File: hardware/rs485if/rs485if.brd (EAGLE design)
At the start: 84.3 x 51 mm, 79 parts, among them IC1 BSP75, IC2 PCA82C250SMD, IC4 78L05SMD, IC5 MAX481CSA, Q1 3M6864, T1 MKDSO_2.5/3_R, T2 MKDSO_2.5/3_R, T3 MKDSO_2.5/3_L, T4 MKDSO_2.5/3_L

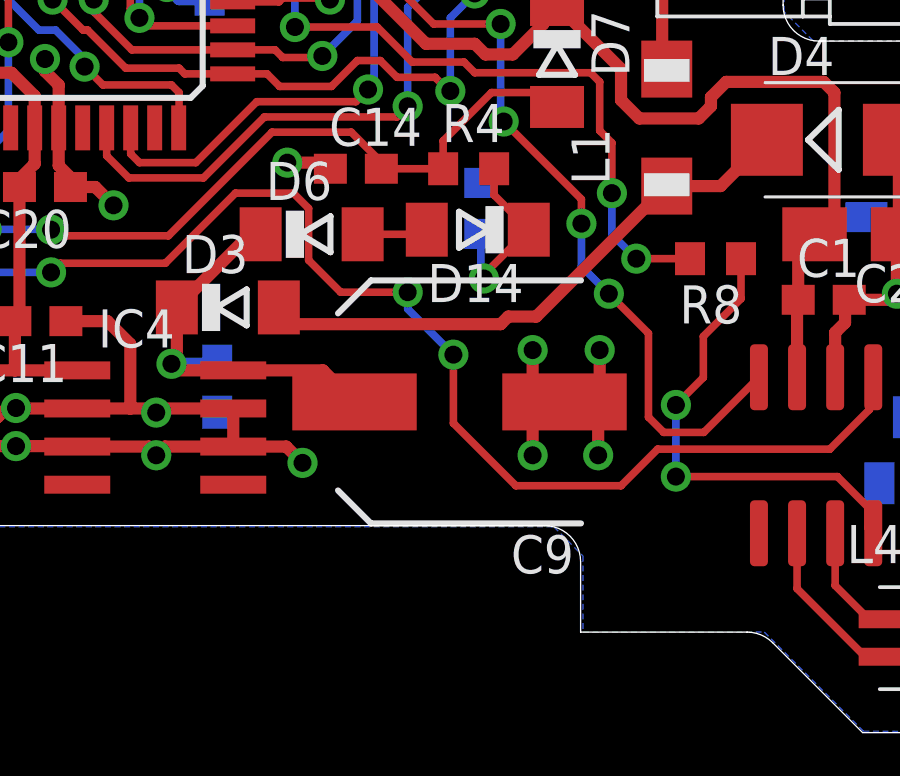
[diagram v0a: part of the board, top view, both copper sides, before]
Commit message: elko position move
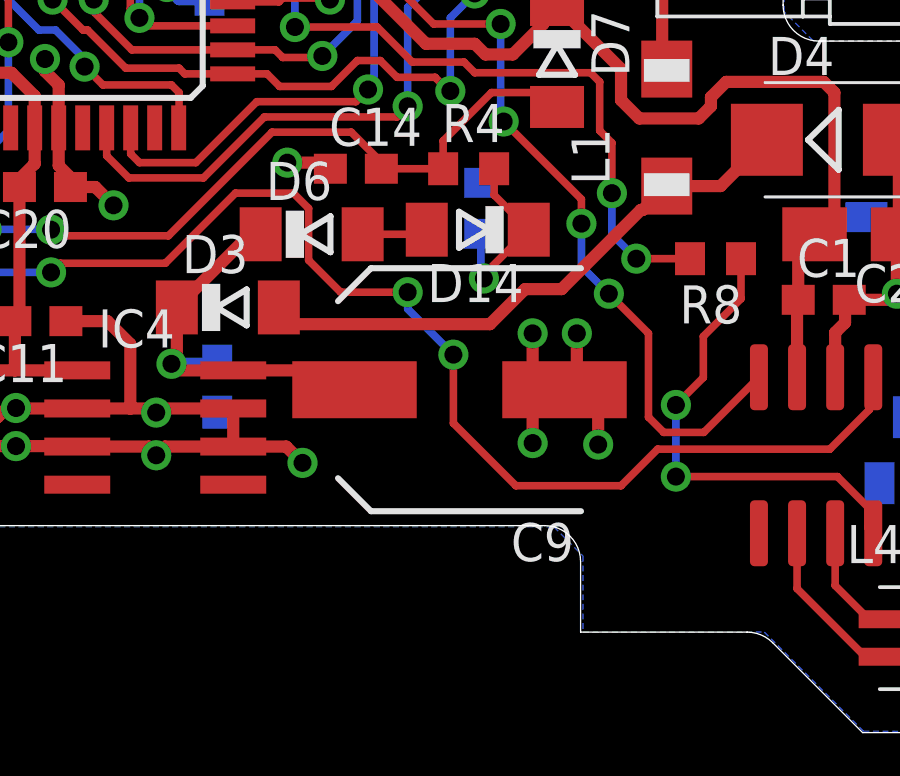
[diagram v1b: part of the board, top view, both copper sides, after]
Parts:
- moved C9 0.41 mm to (52.0, 10.9)
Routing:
- net GND: track 137.6 -> 136.0 mm
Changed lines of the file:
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@@
 <element name="D2" library="EagleLibrary_Wuerth_Elektronik_eiSos_V6_20140807" package="WE-TVS_SOT23-3L" value="WE-TVS_824021" x="66.9676" y="8.8566" rot="MR0"/>
 <element name="IC4" library="linear" package="SO08" value="78L05SMD" x="41.8776" y="9.6112" rot="R270"/>
-<element name="C9" library="rcl" package="SANYO-OSCON_SMD_E7" value="470µ/16V Würth Elektronik WCAP-ASLL 865060353009" x="52.0192" y="10.4648" rot="R180"/>
+<element name="C9" library="rcl" package="SANYO-OSCON_SMD_E7" value="470µ/16V Würth Elektronik WCAP-ASLL 865060353009" x="52.0192" y="10.8712" rot="R180"/>
 <element name="C10" library="resistor" package="C0603" value="100n" x="43.942" y="10.9728" rot="MR90"/>
 <element name="C11" library="resistor" package="C0603" value="100n" x="38.0492" y="13.1572" rot="R180"/>
@@
 <via x="19.9644" y="13.9192" extent="1-16" drill="0.6" shape="octagon"/>
 <via x="66.5988" y="14.0716" extent="1-16" drill="0.6" shape="octagon"/>
-<via x="54.4576" y="8.6868" extent="1-16" drill="0.6" shape="octagon"/>
-<via x="56.642" y="8.6868" extent="1-16" drill="0.6" shape="octagon"/>
-<via x="56.6928" y="12.192" extent="1-16" drill="0.6" shape="octagon"/>
-<via x="54.4576" y="12.192" extent="1-16" drill="0.6" shape="octagon"/>
-<wire x1="54.4576" y1="12.192" x2="54.4576" y2="10.4648" width="0.4064" layer="1"/>
-<wire x1="56.6928" y1="12.192" x2="56.6928" y2="10.4648" width="0.4064" layer="1"/>
-<wire x1="56.6928" y1="10.4648" x2="55.5192" y2="10.4648" width="0.4064" layer="1"/>
-<wire x1="56.642" y1="8.6868" x2="56.642" y2="10.4648" width="0.4064" layer="1"/>
-<wire x1="56.642" y1="10.4648" x2="55.5192" y2="10.4648" width="0.4064" layer="1"/>
-<wire x1="54.4576" y1="8.6868" x2="54.4576" y2="10.4648" width="0.4064" layer="1"/>
-<wire x1="54.4576" y1="10.4648" x2="55.5192" y2="10.4648" width="0.4064" layer="1"/>
+<via x="54.4576" y="9.0932" extent="1-16" drill="0.6" shape="octagon"/>
+<via x="56.642" y="9.0424" extent="1-16" drill="0.6" shape="octagon"/>
+<via x="55.9308" y="12.7508" extent="1-16" drill="0.6" shape="octagon"/>
+<via x="54.4576" y="12.7508" extent="1-16" drill="0.6" shape="octagon"/>
+<wire x1="54.4576" y1="12.7508" x2="54.4576" y2="9.0932" width="0.4064" layer="1"/>
+<wire x1="56.642" y1="9.0424" x2="56.642" y2="10.4648" width="0.4064" layer="1"/>
 <via x="68.7324" y="20.7264" extent="1-16" drill="0.6" shape="octagon"/>
 <via x="37.2364" y="10.2616" extent="1-16" drill="0.6" shape="octagon"/>
@@
 <wire x1="26.0232" y1="47.4472" x2="24.892" y2="47.4472" width="0.4064" layer="1"/>
 <wire x1="35.814" y1="47.9044" x2="34.2392" y2="47.9044" width="0.4064" layer="1"/>
+<wire x1="55.9308" y1="12.7508" x2="55.9308" y2="10.998603125" width="0.4064" layer="1"/>
+<wire x1="55.9308" y1="10.998603125" x2="56.36396875" y2="10.565434375" width="0.4064" layer="1"/>
+<wire x1="56.6928" y1="10.4648" x2="56.642" y2="10.4648" width="0.4064" layer="1"/>
+<wire x1="56.642" y1="10.4648" x2="55.9256" y2="10.4648" width="0.4064" layer="1"/>
+<wire x1="55.9256" y1="10.4648" x2="55.5192" y2="10.8712" width="0.4064" layer="1"/>
 </signal>
 <signal name="N$5">
@@
 <contactref element="L1" pad="1"/>
 <wire x1="45.9976" y1="13.6144" x2="46.5564" y2="13.0556" width="0.4064" layer="1"/>
-<wire x1="46.5564" y1="13.0556" x2="53.3908" y2="13.0556" width="0.4064" layer="1"/>
-<wire x1="53.3908" y1="13.0556" x2="53.6448" y2="13.3096" width="0.4064" layer="1"/>
-<wire x1="53.6448" y1="13.3096" x2="54.5788" y2="13.3096" width="0.4064" layer="1"/>
-<wire x1="54.5788" y1="13.3096" x2="58.928" y2="17.6588" width="0.4064" layer="1"/>
 <wire x1="58.928" y1="17.6588" x2="60.7216" y2="17.6588" width="0.4064" layer="1"/>
 <wire x1="60.7216" y1="17.6588" x2="62.2652" y2="19.2024" width="0.4064" layer="1"/>
+<wire x1="46.5564" y1="13.0556" x2="53.0352" y2="13.0556" width="0.4064" layer="1"/>
+<wire x1="53.0352" y1="13.0556" x2="54.2036" y2="14.224" width="0.4064" layer="1"/>
+<wire x1="54.2036" y1="14.224" x2="55.4228" y2="14.224" width="0.4064" layer="1"/>
+<wire x1="55.4228" y1="14.224" x2="58.0644" y2="16.8656" width="0.4064" layer="1"/>
+<wire x1="58.0644" y1="16.8656" x2="58.1348" y2="16.8656" width="0.4064" layer="1"/>
+<wire x1="58.1348" y1="16.8656" x2="58.928" y2="17.6588" width="0.4064" layer="1"/>
 </signal>
 <signal name="N$3">
@@
 <contactref element="D3" pad="C"/>
 <contactref element="D6" pad="C"/>
-<wire x1="48.5192" y1="10.4648" x2="47.4678" y2="11.5162" width="0.4064" layer="1"/>
-<wire x1="47.4678" y1="11.5162" x2="44.4776" y2="11.5162" width="0.4064" layer="1"/>
+<wire x1="47.8742" y1="11.5162" x2="44.4776" y2="11.5162" width="0.4064" layer="1"/>
 <via x="42.418" y="11.7348" extent="1-16" drill="0.6" shape="octagon"/>
 <wire x1="44.4776" y1="11.5162" x2="42.6366" y2="11.5162" width="0.4064" layer="1"/>
@@
 <wire x1="43.942" y1="11.8228" x2="43.854" y2="11.7348" width="0.4064" layer="16"/>
 <wire x1="43.854" y1="11.7348" x2="42.418" y2="11.7348" width="0.4064" layer="16"/>
+<wire x1="47.8742" y1="11.5162" x2="48.5192" y2="10.8712" width="0.4064" layer="1"/>
 </signal>
 <signal name="B">

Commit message: part value actualization
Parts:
- C14: value (none) -> 10n
- D14, D7: value (none) -> 1N4148
- D6: value 7V5 -> 6V2
- Q1: value 3M6864 -> 18M432
- R4: value (none) -> 100k
- R5: value (none) -> 4k7
- U$3: value (none) -> Atmega1284
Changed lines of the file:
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@@
 <element name="C1" library="resistor" package="C0603" value="100n" x="64.1604" y="13.8684"/>
 <element name="C2" library="rcl" package="A/3216-18W" value="10µ/10V" x="65.3288" y="16.0528" rot="R180"/>
-<element name="Q1" library="crystal" package="SM49" value="3M6864" x="40.5614" y="37.9094">
+<element name="Q1" library="crystal" package="SM49" value="18M432" x="40.5614" y="37.9094">
 <attribute name="OC_NEWARK" value="unknown" x="76.1214" y="-9.0806" size="1.778" layer="27" display="off"/>
 <attribute name="MPN" value="" x="76.1214" y="-9.0806" size="1.778" layer="27" display="off"/>
@@
 <element name="R17" library="resistor" package="R0603" value="10k" x="39.6748" y="42.2148"/>
 <element name="L4" library="EagleLibrary_Wuerth_Elektronik_eiSos_V6_20140807" package="WE-SLM" value="WE744242510" x="68.5292" y="2.5908"/>
-<element name="D7" library="diode" package="SOD80C" value="" x="55.2704" y="21.9964" rot="R270"/>
-<element name="R5" library="resistor" package="R0603" value="" x="52.7304" y="16.9164" rot="MR270"/>
-<element name="C14" library="resistor" package="C0603" value="" x="48.5648" y="18.2372"/>
+<element name="D7" library="diode" package="SOD80C" value="1N4148" x="55.2704" y="21.9964" rot="R270"/>
+<element name="R5" library="resistor" package="R0603" value="4k7" x="52.7304" y="16.9164" rot="MR270"/>
+<element name="C14" library="resistor" package="C0603" value="10n" x="48.5648" y="18.2372"/>
 <element name="IC5" library="maxim" package="SO08" value="MAX481CSA" x="23.0632" y="17.526" rot="R180">
 <attribute name="OC_NEWARK" value="90C3817" x="23.0632" y="17.526" size="1.778" layer="27" rot="R180" display="off"/>
@@
 <element name="C12" library="rcl" package="A/3216-18W" value="10µ/10V" x="20.4724" y="5.1308" rot="R180"/>
 <element name="R3" library="resistor" package="R0603" value="10k" x="31.8008" y="18.8468" rot="R270"/>
-<element name="U$3" library="mylib" package="TQFP44" value="" x="38.6588" y="25.4" rot="R270"/>
+<element name="U$3" library="mylib" package="TQFP44" value="Atmega1284" x="38.6588" y="25.4" rot="R270"/>
 <element name="IC1" library="mylib" package="SOT223" value="BSP75" x="28.3464" y="38.2016"/>
 <element name="R6" library="resistor" package="R0603" value="4k7" x="57.15" y="35.2552" rot="R90"/>
@@
 <element name="R19" library="resistor" package="R0603" value="2k2" x="50.1396" y="41.8084" rot="R270"/>
 <element name="R20" library="resistor" package="R0603" value="2k2" x="45.4152" y="42.2148"/>
-<element name="D6" library="diode" package="SOD80C" value="7V5" x="47.0916" y="16.0528"/>
+<element name="D6" library="diode" package="SOD80C" value="6V2" x="47.0916" y="16.0528"/>
 <element name="JP3" library="pinhead" package="1X02" value="RESET" x="39.2684" y="45.2628"/>
 <element name="U$4" library="mylib" package="GEHÄUSE_PHOENIX_BC_17.8" value="" x="41.656" y="-0.5588"/>
@@
 <element name="C20" library="resistor" package="C0603" value="100n" x="38.2016" y="17.6276" rot="R180"/>
 <element name="SJ1" library="jumper" package="SJ" value="" x="26.924" y="17.9324" rot="MR90"/>
-<element name="R4" library="resistor" package="R0603" value="" x="52.324" y="18.2372"/>
-<element name="D14" library="diode" package="SOD80C" value="" x="52.6288" y="16.2052" rot="R180"/>
+<element name="R4" library="resistor" package="R0603" value="100k" x="52.324" y="18.2372"/>
+<element name="D14" library="diode" package="SOD80C" value="1N4148" x="52.6288" y="16.2052" rot="R180"/>
 <element name="C21" library="resistor" package="C0603" value="100n" x="38.8112" y="31.1404" rot="MR180"/>
 <element name="R11" library="resistor" package="R0603" value="4k7" x="35.7124" y="42.7736" rot="R90"/>
